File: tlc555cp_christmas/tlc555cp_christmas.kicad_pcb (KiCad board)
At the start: 2 copper layers, 58.4 x 99.1 mm, 19 parts, among them SW1 SW_MEC_5E, U1 TLC555xP

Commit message: versior ordered on january 8 2023
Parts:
- C1, C2, R1, R2, R3, R4, R5, R6, R7, U1: moved to B.Cu
- moved C2 23.3 mm to (116.5, 78.0), turned to 180 degrees
- moved R3 20.9 mm to (117.7, 71.9), turned to 180 degrees
- moved C1 19.5 mm to (120.8, 87.4), turned to -90 degrees
- moved U1 8.01 mm to (132.7, 76.6), turned to 180 degrees
- moved R6 4.89 mm to (120.8, 63.6), turned to 0 degrees
- moved D4 1.65 mm to (107.8, 66.3)
- moved G*** 1.55 mm to (117.4, 74.6)
- moved R2 1.36 mm to (122.7, 50.8), turned to -90 degrees
- moved R7 1.27 mm to (108.5, 85.7)
- moved D1 1.18 mm to (116.1, 53.1)
- moved D3 1.17 mm to (121.9, 69.7)
- moved R5 1.15 mm to (106.8, 59.3)
- moved D5 1.03 mm to (100.4, 86.0)
- moved D2 0.98 mm to (125.6, 96.0)
- moved R4 0.62 mm to (128.5, 102.1), turned to 0 degrees
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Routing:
- net GND: track 0.00 -> 221.4 mm
- net output: track 0.00 -> 90.9 mm
- net VCC: track 0.00 -> 84.6 mm
- net Net-(R1-Pad2): track 0.00 -> 43.7 mm
- net Net-(BT1-Pad2): track 0.00 -> 24.9 mm
- net Net-(C2-Pad1): track 0.00 -> 19.3 mm
- net Net-(D4-Pad2): track 0.00 -> 8.45 mm
- net Net-(D3-Pad2): track 0.00 -> 7.62 mm
- net Net-(D2-Pad2): track 0.00 -> 6.25 mm
- net Net-(C1-Pad1): track 0.00 -> 5.62 mm
- net Net-(D5-Pad2): track 0.00 -> 5.58 mm
- net Net-(D1-Pad2): track 0.00 -> 5.03 mm
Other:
- outline, holes or cut-outs redrawn
- board text added: "negative"

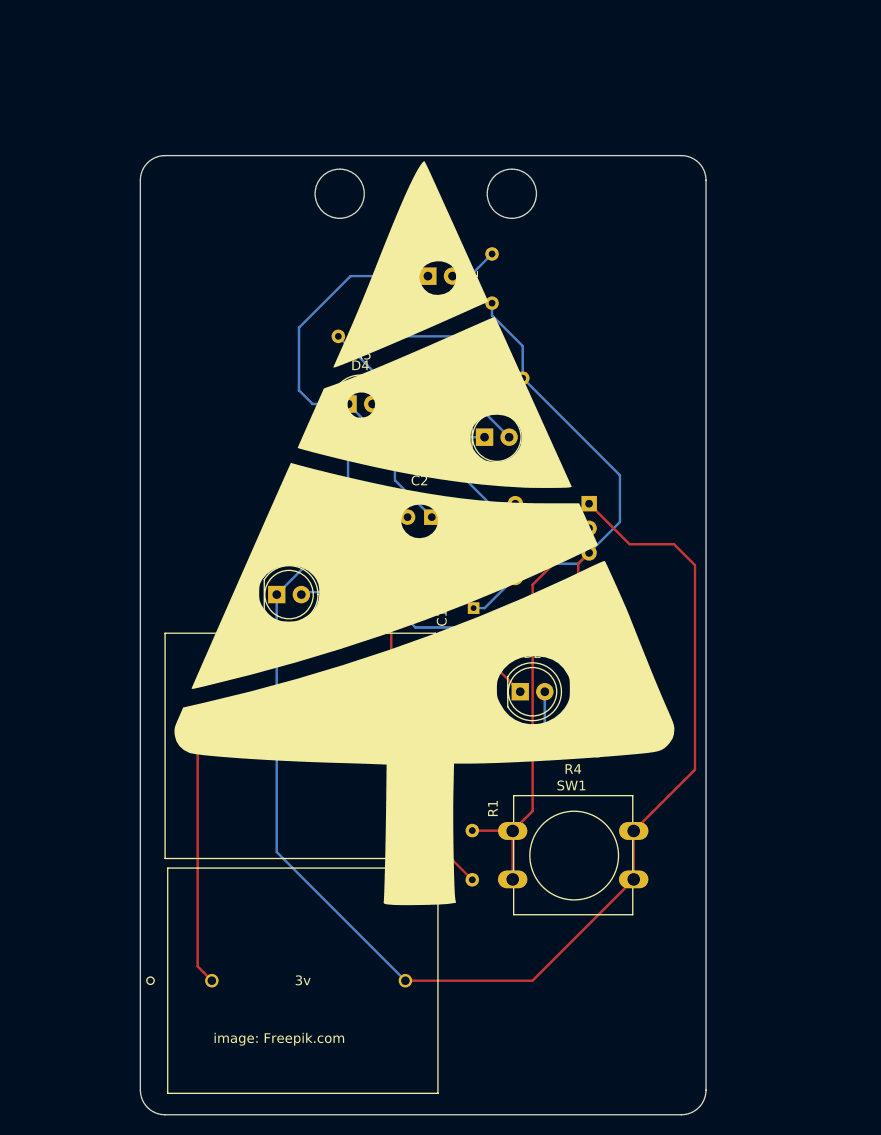
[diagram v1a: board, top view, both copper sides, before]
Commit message: Fix switch footprint pad assignment.
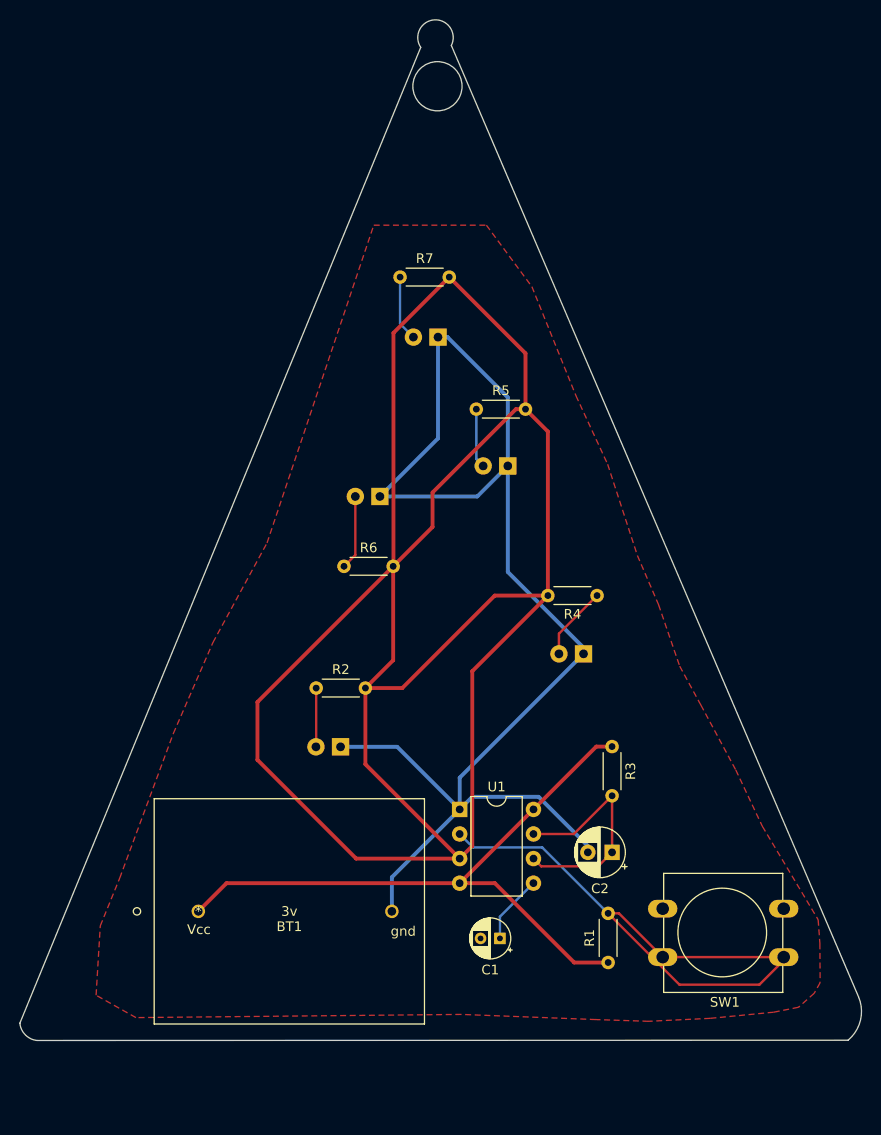
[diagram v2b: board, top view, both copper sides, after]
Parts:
- removed BT2: 3v, footprints:1066
- C1, R1, R2, R4, R5, R6, R7, U1: moved to F.Cu
- C2: value 100u -> 3.3u; moved to F.Cu
- D1, D2, D3, D4, D5, G***: moved to B.Cu
- R3: value 220k -> 10M; moved to F.Cu
- SW1: footprint Button_Switch_THT:SW_PUSH-12mm -> footprints:SW_PUSH-12mm_kody
- moved D1 49.4 mm to (107.0, 101.7), turned to 180 degrees
- moved R2 48.4 mm to (104.5, 95.6), turned to 0 degrees
- moved C2 39.3 mm to (135.1, 112.6)
- moved R3 34.5 mm to (135.1, 101.7), turned to -90 degrees
- moved U1 34.3 mm to (119.3, 108.2), turned to 0 degrees
- moved C1 34.2 mm to (123.5, 121.5), turned to 180 degrees
- moved R7 32.9 mm to (113.2, 53.2)
- moved D5 31.4 mm to (117.1, 59.4), turned to 180 degrees
- moved SW1 30.9 mm to (152.8, 123.4), turned to 180 degrees
- moved BT1 26.3 mm to (92.3, 118.7), turned to 0 degrees
- moved R6 23.6 mm to (107.4, 83.1)
- moved D4 17.7 mm to (124.3, 72.7), turned to 180 degrees
- moved R4 16.8 mm to (133.5, 86.1), turned to 180 degrees
- moved R1 16.4 mm to (134.7, 124.0)
- moved R5 16.1 mm to (121.1, 66.8)
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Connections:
- BT1 pad 2: Net-(BT1-Pad2) -> GND
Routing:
- net output: track 90.9 -> 231.9 mm
- net GND: track 221.4 -> 139.3 mm
- net Net-(BT1-Pad2): track 24.9 -> 0.00 mm
- net Net-(R1-Pad2): track 43.7 -> 61.3 mm
- net VCC: track 84.6 -> 68.5 mm
- net Net-(C2-Pad1): track 19.3 -> 24.6 mm
- net Net-(D4-Pad2): track 8.45 -> 6.16 mm
- net Net-(C1-Pad1): track 5.62 -> 7.14 mm
- net Net-(D2-Pad2): track 6.25 -> 7.65 mm
- net Net-(D5-Pad2): track 5.58 -> 6.77 mm
- net Net-(D1-Pad2): track 5.03 -> 6.08 mm
- added copper zone on F.Cu, net GND
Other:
- board size 58.4 x 99.1 mm -> 86.9 x 105.4 mm
- board text added: "Vcc"
- board text added: "gnd"
- board text removed: "image: Freepik.com"
- board text removed: "negative"
